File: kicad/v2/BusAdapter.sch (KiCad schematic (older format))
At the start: 50 parts, among them J1 Conn_02x17_Odd_Even, J10 Conn_02x06_Odd_Even, J11 Conn_02x02_Odd_Even, J2 Conn_02x20_Odd_Even, J3 Conn_02x20_Odd_Even, J4 Conn_02x06_Top_Bottom, J5 Conn_02x06_Top_Bottom, J6 Conn_Coaxial, J7 Conn_Coaxial, J8 Conn_01x02_Male, J9 Conn_01x02_Male, Q1 2N3904, Q2 2N3904, SW1 SW_Push, SW2 SW_Push, U1 74LVC245, U2 74LVC245, U3 74LVC245, U4 IS61C5128AL-10TLI, U5 MCP4822

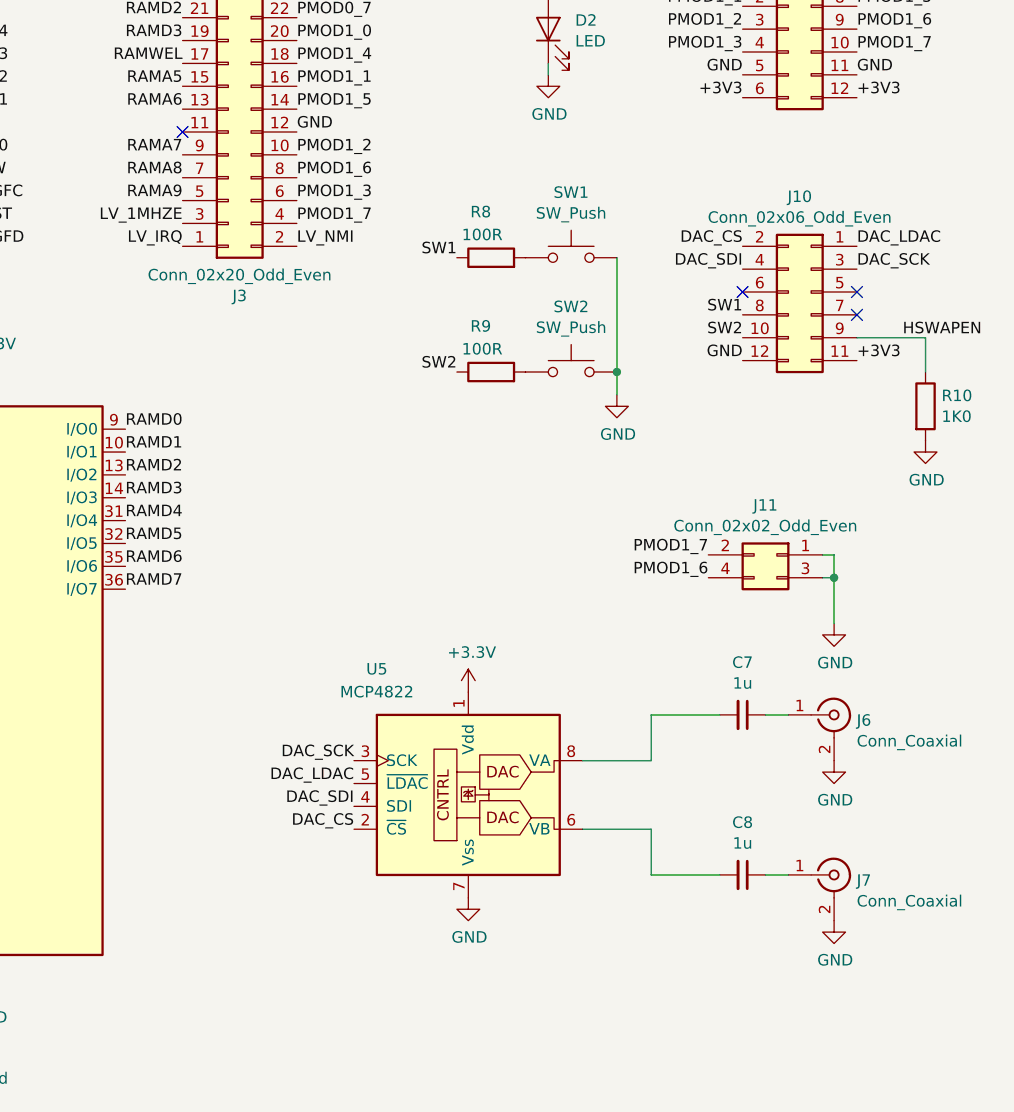
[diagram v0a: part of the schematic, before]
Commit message: PCB v2: Added pmod2 and updated layout
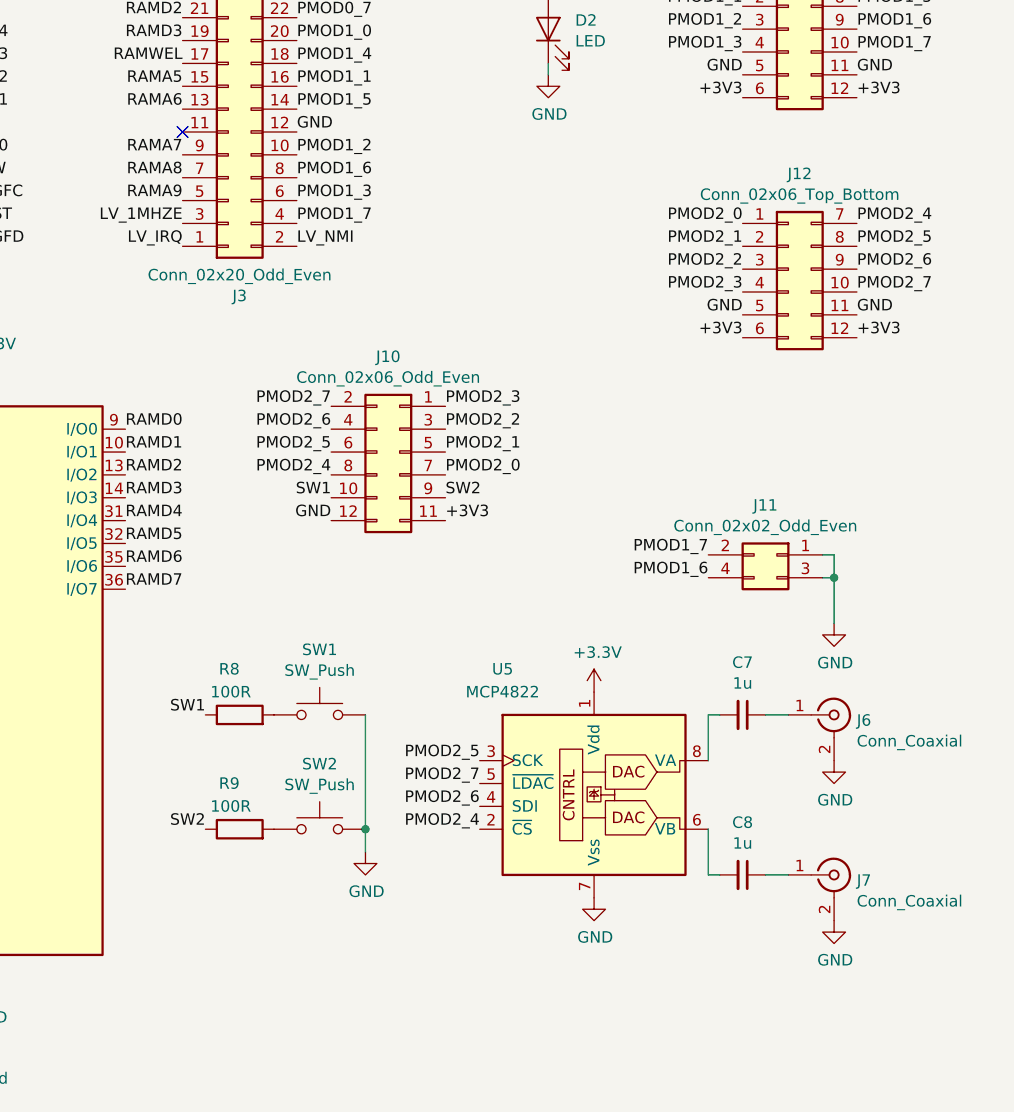
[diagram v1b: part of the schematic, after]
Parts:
- removed R10: 1K0, Resistor_THT:R_Axial_DIN0207_L6.3mm_D2.5mm_P10.16mm_Horizontal, symbol Device:R
- added J12: Conn_02x06_Top_Bottom, footprints:PinSocket_2x06_P2.54mm_Horizontal, symbol Connector_Generic:Conn_02x06_Top_Bottom
- C1, C2, C3, C4, C5: footprint Capacitor_THT:C_Axial_L5.1mm_D3.1mm_P10.00mm_Horizontal -> Capacitor_THT:C_Axial_L3.8mm_D2.6mm_P10.00mm_Horizontal
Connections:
- net HSWAPEN is gone; now on net SW2: J10.9 (Pin_9)
- net +3V3: now also J12.12 (Pin_12), J12.6 (Pin_6)
- net GND: now also J12.11 (Pin_11), J12.5 (Pin_5)
- net SW1: now also J10.10 (Pin_10); no longer J10.8 (Pin_8)
- net SW2: no longer J10.10 (Pin_10)
- net PMOD2_1: now reaches J10.5 (Pin_5)
- net PMOD2_1: now also J12.2 (Pin_2)
- net PMOD2_5: now reaches J10.6 (Pin_6)
- net PMOD2_5: now also U5.3 (SCK), J12.8 (Pin_8)
- net PMOD2_0: now reaches J10.7 (Pin_7)
- net PMOD2_0: now also J12.1 (Pin_1)
- net DAC_CS renamed PMOD2_4
- net PMOD2_4: now also J10.8 (Pin_8), J12.7 (Pin_7); no longer J10.2 (Pin_2)
- net DAC_LDAC renamed PMOD2_3
- net PMOD2_3: now also J12.4 (Pin_4); no longer U5.5 (~LDAC)
- net DAC_SCK renamed PMOD2_2
- net PMOD2_2: now also J12.3 (Pin_3); no longer U5.3 (SCK)
- net DAC_SDI renamed PMOD2_6
- net PMOD2_6: now also J12.9 (Pin_9)
- new net PMOD2_7: J10.2 (Pin_2), J12.10 (Pin_10), U5.5 (~LDAC)
- no-connect marks 21 -> 18
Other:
- moved on the sheet: J10, R8, R9, SW1, SW2, U5

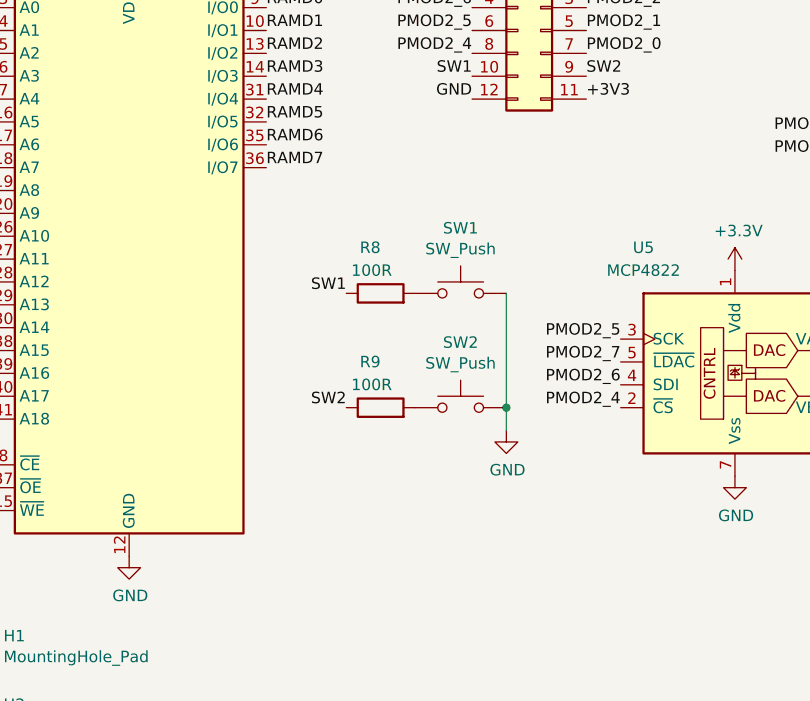
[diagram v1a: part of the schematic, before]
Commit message: PCB v2: Updated SW1/2 to HSWAPEN pulled low on power up
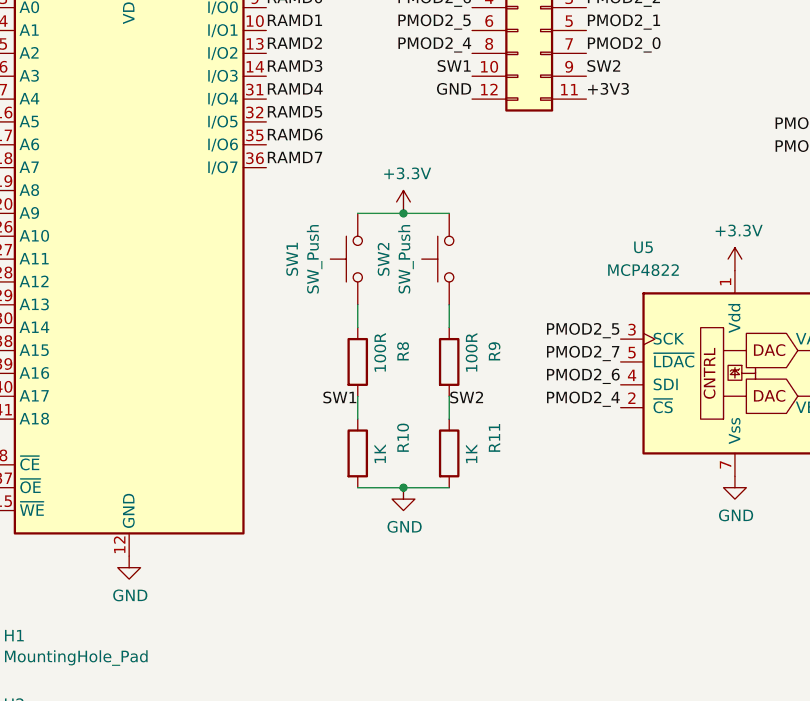
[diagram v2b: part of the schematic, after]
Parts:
- added R10, R11: 1K, Resistor_THT:R_Axial_DIN0207_L6.3mm_D2.5mm_P10.16mm_Horizontal, symbol Device:R
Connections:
- net +3V3: now also SW1.2, SW2.2
- net GND: now also R10.2, R11.2; no longer SW1.2, SW2.2
- net SW1: now also R8.2, R10.1; no longer R8.1
- net SW2: now also R9.2, R11.1; no longer R9.1
- net at SW1.1: now also R8.1; no longer R8.2
- net at SW2.1: now also R9.1; no longer R9.2
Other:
- moved on the sheet: R8, R9, SW1, SW2
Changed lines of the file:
@@
 L Switch:SW_Push SW1
 U 1 1 5C7C4C64
-P 8150 5100
-F 0 "SW1" H 8150 5385 50  0000 C CNN
-F 1 "SW_Push" H 8150 5294 50  0000 C CNN
-F 2 "Button_Switch_THT:SW_PUSH_6mm_H5mm" H 8150 5300 50  0001 C CNN
-F 3 "" H 8150 5300 50  0001 C CNN
-	1    8150 5100
-	1    0    0    -1
+P 7700 4950
+F 0 "SW1" H 7700 5235 50  0000 C CNN
+F 1 "SW_Push" H 7700 5144 50  0000 C CNN
+F 2 "Button_Switch_THT:SW_PUSH_6mm_H5mm" H 7700 5150 50  0001 C CNN
+F 3 "" H 7700 5150 50  0001 C CNN
+	1    7700 4950
+	0    -1   -1   0
 $EndComp
 $Comp
 L Switch:SW_Push SW2
 U 1 1 5C7C4D3E
-P 8150 5600
-F 0 "SW2" H 8150 5885 50  0000 C CNN
-F 1 "SW_Push" H 8150 5794 50  0000 C CNN
-F 2 "Button_Switch_THT:SW_PUSH_6mm_H5mm" H 8150 5800 50  0001 C CNN
-F 3 "" H 8150 5800 50  0001 C CNN
-	1    8150 5600
-	1    0    0    -1
-$EndComp
-Text Label 7650 5100 2    50   ~ 0
-SW1
-Text Label 7650 5600 2    50   ~ 0
+P 8100 4950
+F 0 "SW2" H 8100 5235 50  0000 C CNN
+F 1 "SW_Push" H 8100 5144 50  0000 C CNN
+F 2 "Button_Switch_THT:SW_PUSH_6mm_H5mm" H 8100 5150 50  0001 C CNN
+F 3 "" H 8100 5150 50  0001 C CNN
+	1    8100 4950
+	0    -1   -1   0
+$EndComp
+Text Label 8100 5600 0    50   ~ 0
 SW2
-Wire Wire Line
-	8350 5100 8350 5600
-$Comp
-L power:GND #PWR021
-U 1 1 5C7C7AF9
-P 8350 5700
-F 0 "#PWR021" H 8350 5450 50  0001 C CNN
-F 1 "GND" H 8355 5527 50  0000 C CNN
-F 2 "" H 8350 5700 50  0001 C CNN
-F 3 "" H 8350 5700 50  0001 C CNN
-	1    8350 5700
-	1    0    0    -1
-$EndComp
-Wire Wire Line
-	8350 5600 8350 5700
-Connection ~ 8350 5600
 $Comp
 L Device:R R8
 U 1 1 5C7D1F77
-P 7800 5100
-F 0 "R8" V 8000 5100 50  0000 L CNN
-F 1 "100R" V 7900 5050 50  0000 L CNN
-F 2 "Resistor_THT:R_Axial_DIN0207_L6.3mm_D2.5mm_P10.16mm_Horizontal" V 7730 5100 50  0001 C CNN
-F 3 "~" H 7800 5100 50  0001 C CNN
-	1    7800 5100
-	0    -1   -1   0
+P 7700 5400
+F 0 "R8" V 7900 5400 50  0000 L CNN
+F 1 "100R" V 7800 5350 50  0000 L CNN
+F 2 "Resistor_THT:R_Axial_DIN0207_L6.3mm_D2.5mm_P10.16mm_Horizontal" V 7630 5400 50  0001 C CNN
+F 3 "~" H 7700 5400 50  0001 C CNN
+	1    7700 5400
+	1    0    0    -1
 $EndComp
 $Comp
 L Device:R R9
 U 1 1 5C7D51EB
-P 7800 5600
-F 0 "R9" V 8000 5600 50  0000 L CNN
-F 1 "100R" V 7900 5550 50  0000 L CNN
-F 2 "Resistor_THT:R_Axial_DIN0207_L6.3mm_D2.5mm_P10.16mm_Horizontal" V 7730 5600 50  0001 C CNN
-F 3 "~" H 7800 5600 50  0001 C CNN
-	1    7800 5600
-	0    -1   -1   0
+P 8100 5400
+F 0 "R9" V 8300 5400 50  0000 L CNN
+F 1 "100R" V 8200 5350 50  0000 L CNN
+F 2 "Resistor_THT:R_Axial_DIN0207_L6.3mm_D2.5mm_P10.16mm_Horizontal" V 8030 5400 50  0001 C CNN
+F 3 "~" H 8100 5400 50  0001 C CNN
+	1    8100 5400
+	1    0    0    -1
 $EndComp
 $Comp
@@
 Text Label 8850 5400 2    50   ~ 0
 PMOD2_7
+Wire Wire Line
+	8100 5150 8100 5250
+Text Label 7700 5600 2    50   ~ 0
+SW1
+Wire Wire Line
+	7700 5150 7700 5250
+$Comp
+L Device:R R10
+U 1 1 5CA628B7
+P 7700 5800
+F 0 "R10" V 7900 5800 50  0000 L CNN
+F 1 "1K" V 7800 5750 50  0000 L CNN
+F 2 "Resistor_THT:R_Axial_DIN0207_L6.3mm_D2.5mm_P10.16mm_Horizontal" V 7630 5800 50  0001 C CNN
+F 3 "~" H 7700 5800 50  0001 C CNN
+	1    7700 5800
+	1    0    0    -1
+$EndComp
+$Comp
+L Device:R R11
+U 1 1 5CA629EB
+P 8100 5800
+F 0 "R11" V 8300 5800 50  0000 L CNN
+F 1 "1K" V 8200 5750 50  0000 L CNN
+F 2 "Resistor_THT:R_Axial_DIN0207_L6.3mm_D2.5mm_P10.16mm_Horizontal" V 8030 5800 50  0001 C CNN
+F 3 "~" H 8100 5800 50  0001 C CNN
+	1    8100 5800
+	1    0    0    -1
+$EndComp
+Wire Wire Line
+	7700 5550 7700 5650
+Wire Wire Line
+	8100 5550 8100 5650
+Wire Wire Line
+	7700 5950 7900 5950
+Wire Wire Line
+	8100 4750 7900 4750
+$Comp
+L power:+3.3V #PWR021
+U 1 1 5CA6DACB
+P 7900 4750
+F 0 "#PWR021" H 7900 4600 50  0001 C CNN
+F 1 "+3.3V" H 7915 4923 50  0000 C CNN
+F 2 "" H 7900 4750 50  0001 C CNN
+F 3 "" H 7900 4750 50  0001 C CNN
+	1    7900 4750
+	1    0    0    -1
+$EndComp
+Connection ~ 7900 4750
+Wire Wire Line
+	7900 4750 7700 4750
+$Comp
+L power:GND #PWR022
+U 1 1 5CA6DB40
+P 7900 5950
+F 0 "#PWR022" H 7900 5700 50  0001 C CNN
+F 1 "GND" H 7905 5777 50  0000 C CNN
+F 2 "" H 7900 5950 50  0001 C CNN
+F 3 "" H 7900 5950 50  0001 C CNN
+	1    7900 5950
+	1    0    0    -1
+$EndComp
+Connection ~ 7900 5950
+Wire Wire Line
+	7900 5950 8100 5950
 $EndSCHEMATC

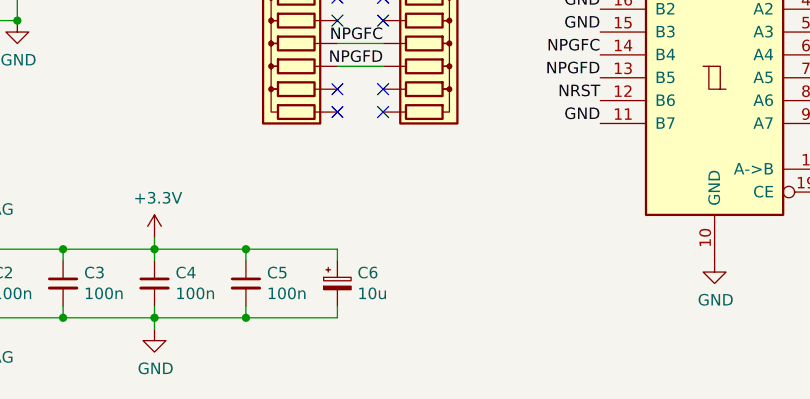
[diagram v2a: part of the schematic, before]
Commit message: PCB v2: Improved SRAM decoupling
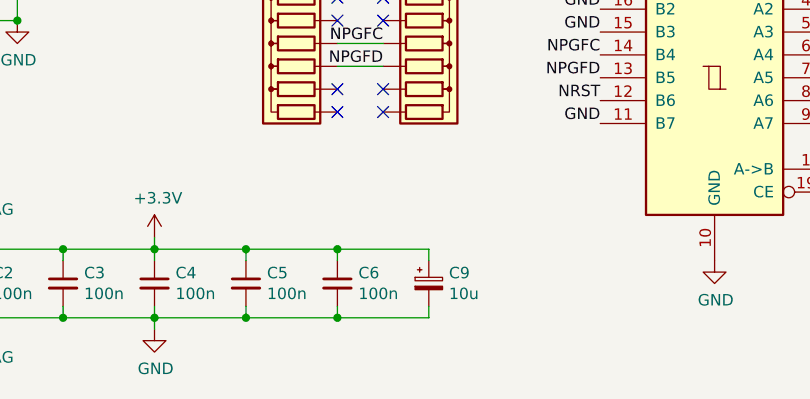
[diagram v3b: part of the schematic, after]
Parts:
- added C6: 100n, Capacitor_THT:C_Axial_L3.8mm_D2.6mm_P7.50mm_Horizontal, symbol Device:C_Small
- C5: footprint Capacitor_THT:C_Axial_L3.8mm_D2.6mm_P10.00mm_Horizontal -> Capacitor_THT:C_Axial_L3.8mm_D2.6mm_P7.50mm_Horizontal
- renumbered C6 to C9
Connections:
- net +3V3: now also C6.1
- net GND: now also C6.2
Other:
- moved on the sheet: C9
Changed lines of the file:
@@
 F 0 "C5" H 2542 7346 50  0000 L CNN
 F 1 "100n" H 2542 7255 50  0000 L CNN
-F 2 "Capacitor_THT:C_Axial_L3.8mm_D2.6mm_P10.00mm_Horizontal" H 2450 7300 50  0001 C CNN
+F 2 "Capacitor_THT:C_Axial_L3.8mm_D2.6mm_P7.50mm_Horizontal" H 2450 7300 50  0001 C CNN
 F 3 "~" H 2450 7300 50  0001 C CNN
 	1    2450 7300
@@
 	2850 7450 2850 7400
 Wire Wire Line
-	2850 7150 2850 7200
-Wire Wire Line
-	2450 7150 2850 7150
-Wire Wire Line
 	2450 7450 2850 7450
 Connection ~ 2450 7150
@@
 NoConn ~ 1200 2050
 $Comp
-L Device:CP_Small C6
+L Device:CP_Small C9
 U 1 1 5C7A0AD1
-P 2850 7300
-F 0 "C6" H 2938 7346 50  0000 L CNN
-F 1 "10u" H 2938 7255 50  0000 L CNN
-F 2 "Capacitor_THT:CP_Radial_D5.0mm_P2.50mm" H 2850 7300 50  0001 C CNN
-F 3 "~" H 2850 7300 50  0001 C CNN
-	1    2850 7300
+P 3250 7300
+F 0 "C9" H 3338 7346 50  0000 L CNN
+F 1 "10u" H 3338 7255 50  0000 L CNN
+F 2 "Capacitor_THT:CP_Radial_D5.0mm_P2.50mm" H 3250 7300 50  0001 C CNN
+F 3 "~" H 3250 7300 50  0001 C CNN
+	1    3250 7300
 	1    0    0    -1
 $EndComp
@@
 Wire Wire Line
 	7900 5950 8100 5950
+$Comp
+L Device:C_Small C6
+U 1 1 5CA6EEE6
+P 2850 7300
+F 0 "C6" H 2942 7346 50  0000 L CNN
+F 1 "100n" H 2942 7255 50  0000 L CNN
+F 2 "Capacitor_THT:C_Axial_L3.8mm_D2.6mm_P7.50mm_Horizontal" H 2850 7300 50  0001 C CNN
+F 3 "~" H 2850 7300 50  0001 C CNN
+	1    2850 7300
+	1    0    0    -1
+$EndComp
+Wire Wire Line
+	3250 7150 3250 7200
+Wire Wire Line
+	2850 7150 3250 7150
+Wire Wire Line
+	2450 7150 2850 7150
+Connection ~ 2850 7150
+Wire Wire Line
+	2850 7150 2850 7200
+Wire Wire Line
+	2850 7450 3250 7450
+Wire Wire Line
+	3250 7450 3250 7400
+Connection ~ 2850 7450
 $EndSCHEMATC
